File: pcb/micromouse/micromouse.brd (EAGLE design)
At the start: 81.5 x 99.2 mm, 57 parts, among them J1 Connector_M1, J2 Connector_M2, J4 Programmer

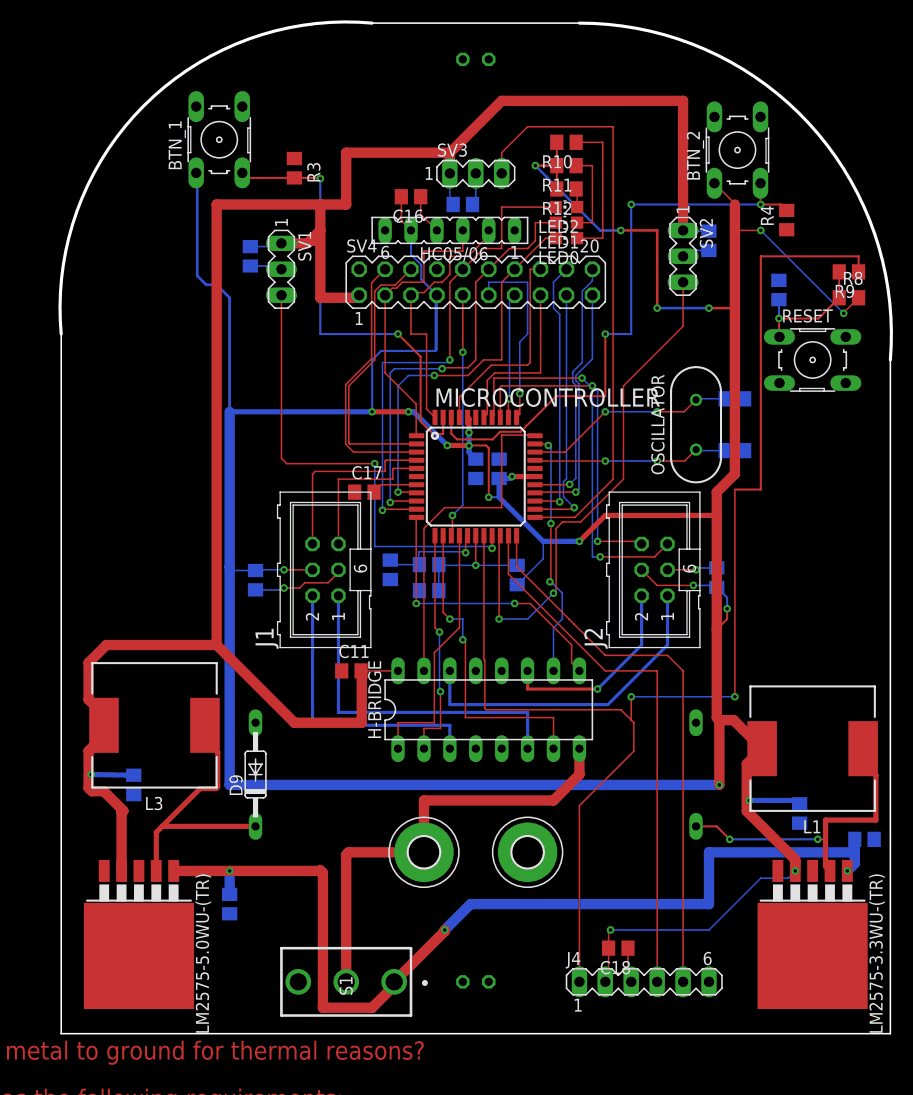
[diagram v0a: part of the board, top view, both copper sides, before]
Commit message: Exchanged 100 uF capacitors at voltage regulator to have 1210 mounting layout + added ground planes
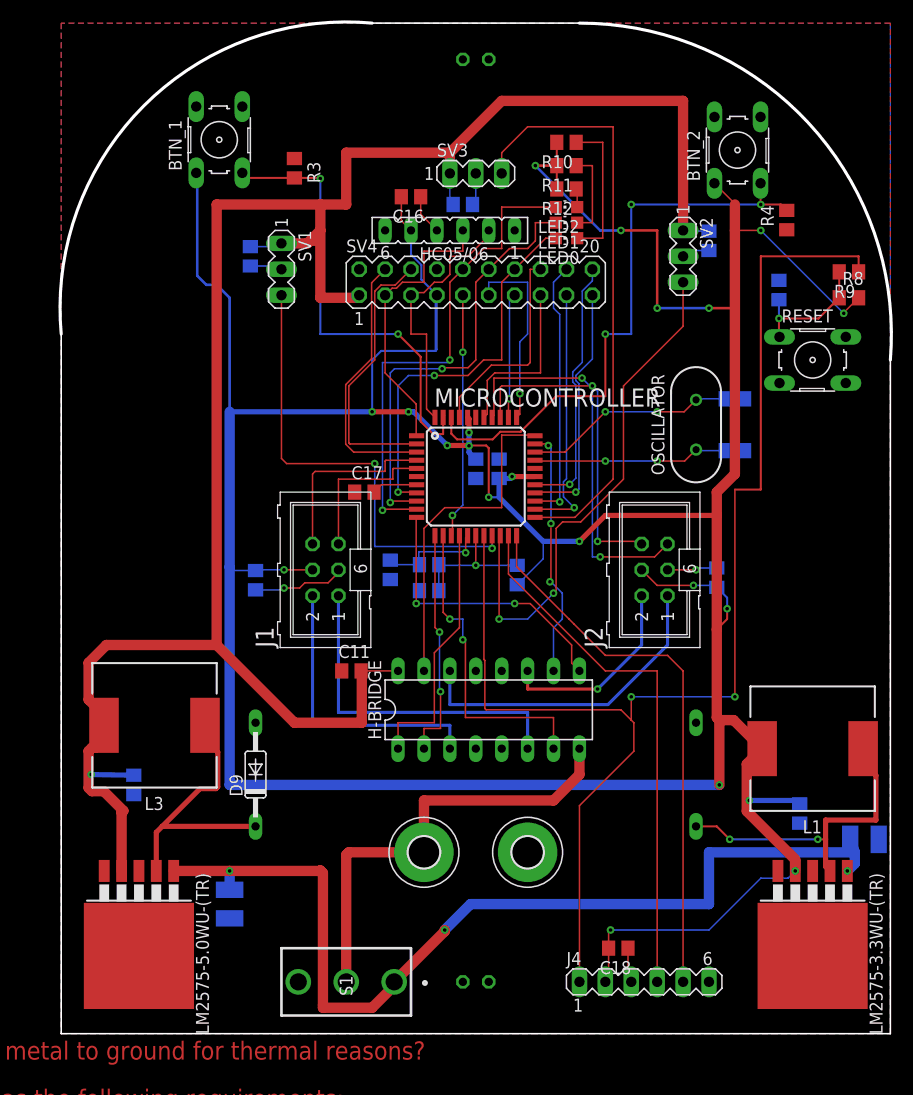
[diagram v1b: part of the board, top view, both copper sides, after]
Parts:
- C12, C14: device rcl:C0805 -> rcl:C1210
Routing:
- added copper zone on layer 1, net GND
- added copper zone on layer 16, net GND
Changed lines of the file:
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@@
 <attribute name="VALUE" x="27.178" y="33.02" size="1.27" layer="27"/>
 </element>
-<element name="C12" library="rcl" library_urn="urn:adsk.eagle:library:334" package="C0805" package3d_urn="urn:adsk.eagle:package:23617/2" value="100uF" x="16.51" y="12.7" smashed="yes" rot="MR90">
+<element name="C12" library="rcl" library_urn="urn:adsk.eagle:library:334" package="C1210" package3d_urn="urn:adsk.eagle:package:23619/2" value="100uF" x="16.51" y="12.7" smashed="yes" rot="MR90">
 <attribute name="NAME" x="17.78" y="11.43" size="1.27" layer="26" rot="MR90"/>
-<attribute name="POPULARITY" value="88" x="-53.34" y="43.18" size="1.778" layer="28" rot="MR90" display="off"/>
+<attribute name="POPULARITY" value="0" x="-53.34" y="43.18" size="1.778" layer="28" rot="MR90" display="off"/>
 <attribute name="SPICEPREFIX" value="C" x="-53.34" y="43.18" size="1.778" layer="28" rot="MR90" display="off"/>
 <attribute name="VALUE" x="13.97" y="11.43" size="1.27" layer="28" rot="MR90"/>
@@
 <attribute name="VALUE" x="4.572" y="23.114" size="1.27" layer="28" rot="MR90"/>
 </element>
-<element name="C14" library="rcl" library_urn="urn:adsk.eagle:library:334" package="C0805" package3d_urn="urn:adsk.eagle:package:23617/2" value="100uF" x="78.74" y="19.05" smashed="yes" rot="MR0">
+<element name="C14" library="rcl" library_urn="urn:adsk.eagle:library:334" package="C1210" package3d_urn="urn:adsk.eagle:package:23619/2" value="100uF" x="78.74" y="19.05" smashed="yes" rot="MR0">
 <attribute name="NAME" x="80.01" y="20.32" size="1.27" layer="26" rot="MR0"/>
-<attribute name="POPULARITY" value="88" x="35.56" y="-50.8" size="1.778" layer="28" rot="MR0" display="off"/>
+<attribute name="POPULARITY" value="0" x="35.56" y="-50.8" size="1.778" layer="28" rot="MR0" display="off"/>
 <attribute name="SPICEPREFIX" value="C" x="35.56" y="-50.8" size="1.778" layer="28" rot="MR0" display="off"/>
 <attribute name="VALUE" x="80.01" y="16.51" size="1.27" layer="28" rot="MR0"/>
@@
 <wire x1="27.178" y1="45.212" x2="27.178" y2="45.466" width="0.1524" layer="1"/>
 <wire x1="42.54" y1="56.322" x2="42.926" y2="56.322" width="0.2" layer="16"/>
-<wire x1="70.358" y1="73.848" x2="71.12" y2="78.806" width="0" layer="19" extent="1-16"/>
-<wire x1="63.5" y1="76.774" x2="70.358" y2="73.848" width="0" layer="19" extent="16-16"/>
-<wire x1="70.4088" y1="63.7794" x2="70.358" y2="73.848" width="0" layer="19" extent="16-16"/>
-<wire x1="66.99" y1="62.23" x2="70.4088" y2="63.7794" width="0" layer="19" extent="16-16"/>
-<wire x1="66.99" y1="57.15" x2="66.99" y2="62.23" width="0" layer="19" extent="16-16"/>
-<wire x1="64.262" y1="45.654" x2="66.99" y2="57.15" width="0" layer="19" extent="16-16"/>
-<wire x1="62.23" y1="30.48" x2="62.23" y2="45.466" width="0" layer="19" extent="1-1"/>
-<wire x1="72.39" y1="20.64" x2="62.23" y2="30.48" width="0" layer="19" extent="16-16"/>
-<wire x1="73.66" y1="15.9512" x2="72.39" y2="20.64" width="0" layer="19" extent="1-16"/>
-<wire x1="70.2564" y1="15.9512" x2="73.66" y2="15.9512" width="0" layer="19" extent="1-1"/>
-<wire x1="79.69" y1="19.05" x2="73.66" y2="15.9512" width="0" layer="19" extent="1-16"/>
-<wire x1="46.44" y1="55.41" x2="59.436" y2="45.466" width="0" layer="19" extent="1-1"/>
-<wire x1="42.992" y1="56.388" x2="46.402" y2="55.372" width="0" layer="19" extent="1-16"/>
-<wire x1="40.64" y1="54.422" x2="42.54" y2="56.322" width="0" layer="19" extent="16-16"/>
-<wire x1="40.64" y1="60.41" x2="42.54" y2="56.322" width="0" layer="19" extent="1-16"/>
+<polygon width="0.1524" layer="16">
+<vertex x="0" y="0"/>
+<vertex x="81.28" y="0"/>
+<vertex x="81.28" y="71.12"/>
+<vertex x="81.28" y="99.06"/>
+<vertex x="0" y="99.06"/>
+</polygon>
+<polygon width="0.1524" layer="1">
+<vertex x="0" y="0"/>
+<vertex x="81.28" y="0"/>
+<vertex x="81.28" y="99.06"/>
+<vertex x="0" y="99.06"/>
+</polygon>
+<wire x1="46.402" y1="55.372" x2="42.992" y2="56.388" width="0" layer="19" extent="1-16"/>
 <wire x1="34.84" y1="54.61" x2="40.64" y2="54.422" width="0" layer="19" extent="1-16"/>
-<wire x1="28.768" y1="53.086" x2="34.84" y2="54.61" width="0" layer="19" extent="1-1"/>
-<wire x1="27.178" y1="45.466" x2="28.768" y2="53.086" width="0" layer="19" extent="1-1"/>
-<wire x1="32.258" y1="44.516" x2="27.178" y2="45.466" width="0" layer="19" extent="16-16"/>
-<wire x1="35.118" y1="43.434" x2="32.258" y2="44.516" width="0" layer="19" extent="16-16"/>
-<wire x1="40.64" y1="35.56" x2="35.118" y2="43.434" width="0" layer="19" extent="16-16"/>
-<wire x1="43.18" y1="35.56" x2="40.64" y2="35.56" width="0" layer="19" extent="1-1"/>
-<wire x1="43.18" y1="27.94" x2="43.18" y2="35.56" width="0" layer="19" extent="1-1"/>
-<wire x1="40.64" y1="27.94" x2="43.18" y2="27.94" width="0" layer="19" extent="1-1"/>
-<wire x1="27.498" y1="35.56" x2="21.844" y2="43.688" width="0" layer="19" extent="1-1"/>
-<wire x1="19.05" y1="30.48" x2="27.498" y2="35.56" width="0" layer="19" extent="1-1"/>
-<wire x1="45.72" y1="17.78" x2="43.18" y2="27.94" width="0" layer="19" extent="1-1"/>
-<wire x1="55.56" y1="8.382" x2="45.72" y2="17.78" width="0" layer="19" extent="1-1"/>
-<wire x1="7.112" y1="23.434" x2="19.05" y2="30.48" width="0" layer="19" extent="16-16"/>
-<wire x1="7.62" y1="15.9512" x2="7.112" y2="23.434" width="0" layer="19" extent="1-16"/>
-<wire x1="4.2164" y1="15.9512" x2="7.62" y2="15.9512" width="0" layer="19" extent="1-1"/>
-<wire x1="16.51" y1="11.75" x2="7.62" y2="15.9512" width="0" layer="19" extent="1-16"/>
-<wire x1="36.83" y1="74.93" x2="40.64" y2="60.41" width="0" layer="19" extent="1-1"/>
-<wire x1="36.83" y1="78.74" x2="36.83" y2="74.93" width="0" layer="19" extent="1-1"/>
-<wire x1="40.32" y1="81.28" x2="36.83" y2="78.74" width="0" layer="19" extent="16-16"/>
-<wire x1="29.21" y1="74.93" x2="36.83" y2="74.93" width="0" layer="19" extent="1-1"/>
-<wire x1="21.59" y1="74.93" x2="29.21" y2="74.93" width="0" layer="19" extent="1-1"/>
-<wire x1="22.86" y1="85.786" x2="21.59" y2="74.93" width="0" layer="19" extent="1-1"/>
 </signal>
 <signal name="AVDD">
@@
 <contactref element="C14" pad="2"/>
 <contactref element="S1" pad="1"/>
-<wire x1="77.79" y1="19.05" x2="77.536" y2="18.796" width="0.508" layer="16"/>
+<wire x1="77.34" y1="19.05" x2="77.536" y2="18.796" width="0.508" layer="16"/>
 <wire x1="25.4" y1="2.794" x2="25.654" y2="2.54" width="0.508" layer="1"/>
-<wire x1="77.79" y1="19.05" x2="77.79" y2="17.78" width="1.016" layer="16"/>
+<wire x1="77.34" y1="19.05" x2="77.79" y2="17.78" width="1.016" layer="16"/>
 <wire x1="77.79" y1="17.78" x2="77.79" y2="16.6776" width="1.016" layer="16"/>
 <wire x1="77.79" y1="16.6776" x2="77.0636" y2="15.9512" width="1.016" layer="16"/>
@@
 <wire x1="30.48" y1="2.54" x2="32.64" y2="4.7" width="1.016" layer="1"/>
 <wire x1="32.64" y1="4.7" x2="32.64" y2="5.08" width="1.016" layer="1"/>
-<wire x1="16.51" y1="13.65" x2="16.51" y2="15.9512" width="1.016" layer="16"/>
+<wire x1="16.51" y1="14.1" x2="16.51" y2="15.9512" width="1.016" layer="16"/>
 <via x="16.51" y="15.9512" extent="1-16" drill="0.35"/>
 <wire x1="32.64" y1="5.08" x2="37.592" y2="10.032" width="1.016" layer="1"/>

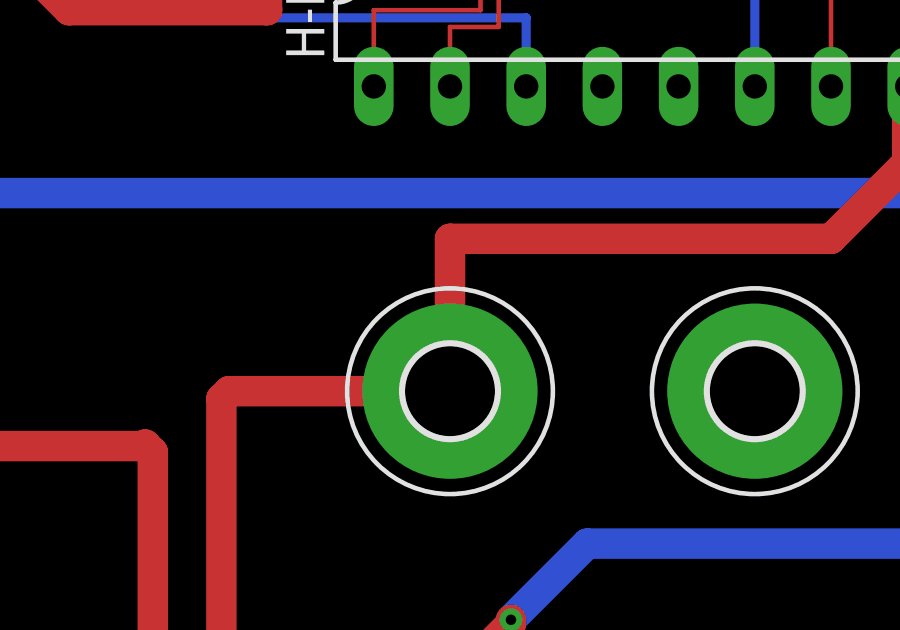
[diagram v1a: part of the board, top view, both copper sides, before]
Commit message: Fix positioning of power switch.
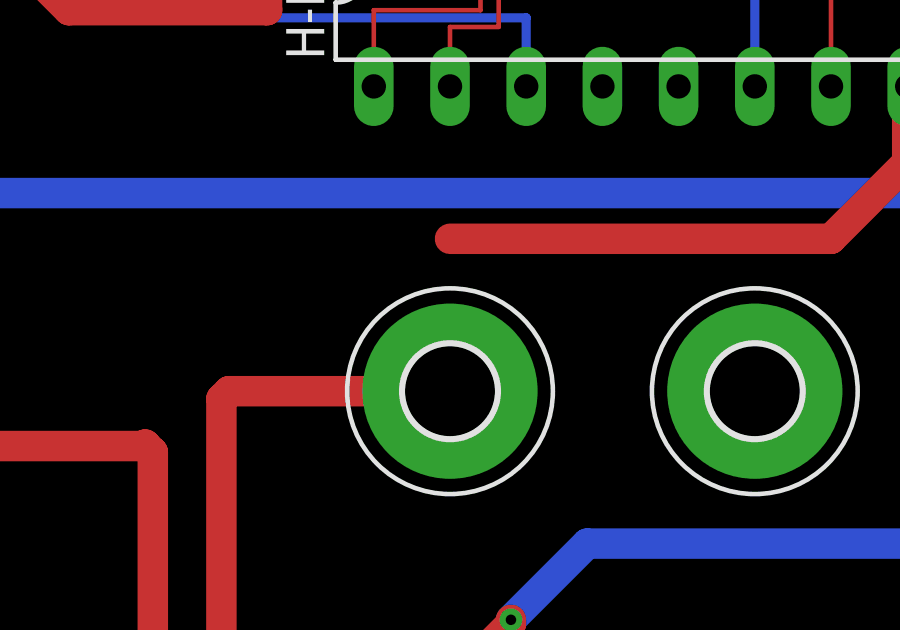
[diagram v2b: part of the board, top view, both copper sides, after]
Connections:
- removed net N$3: C12.2, C14.2, LM2575-3.3WU-(TR).1, LM2575-5.0WU-(TR).1, S1.1
- new net N$2: +9V.B3,0, S1.2
- net +9V: now also C12.2, C14.2, LM2575-3.3WU-(TR).1, LM2575-5.0WU-(TR).1, S1.1; no longer +9V.B3,0, S1.2
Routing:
- net N$3: track 95.7 -> 0.00 mm, vias 3 -> 0
- net +9V: track 44.1 -> 114.5 mm, vias 0 -> 3
- net N$2: track 0.00 -> 20.2 mm
